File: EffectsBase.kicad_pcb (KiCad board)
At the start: 2 copper layers, 59 x 98 mm, 31 parts, among them J1 JACK CONNECTOR, J2 FOOTSWITCH, J3 PCIE_FX, Q1 SI2301BDS, SW1 SW_SPDT, SW2 SW_SPDT, SW3 MINI_SW, SW4 MINI_SW, U1 ICL7660S

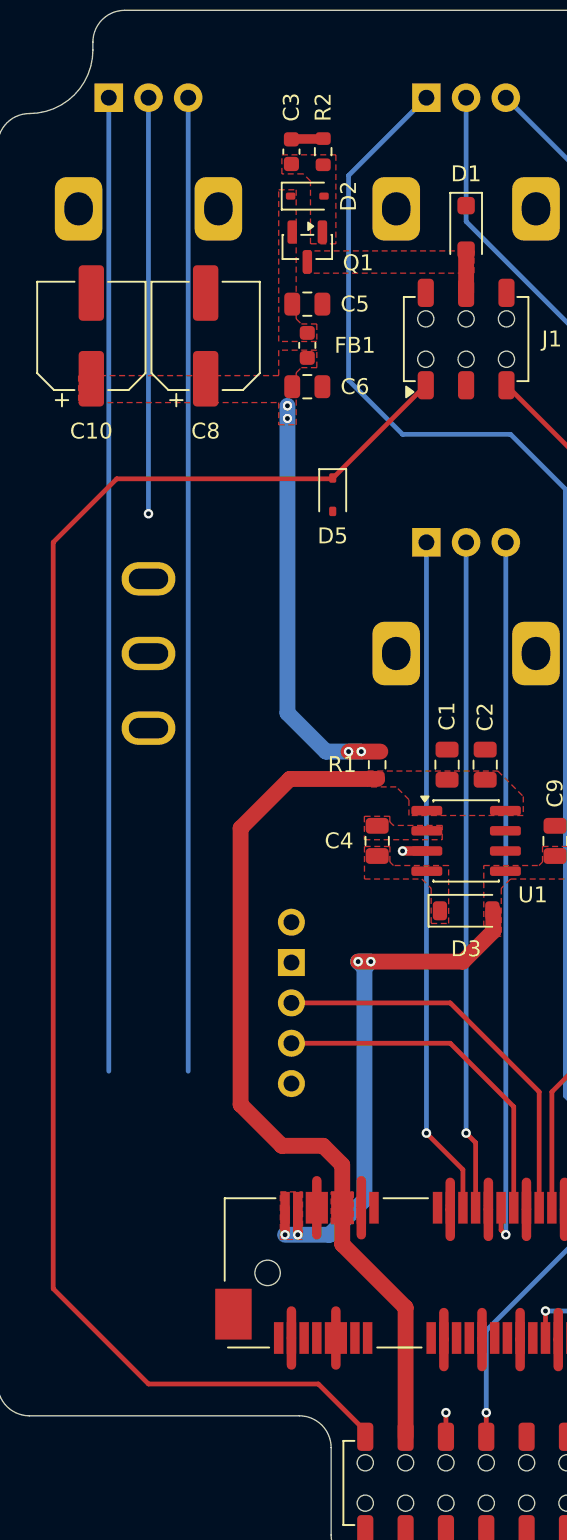
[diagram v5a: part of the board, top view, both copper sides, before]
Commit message: Board layout
Updated the layout of the power lines.
Updated the layout of the control signals.
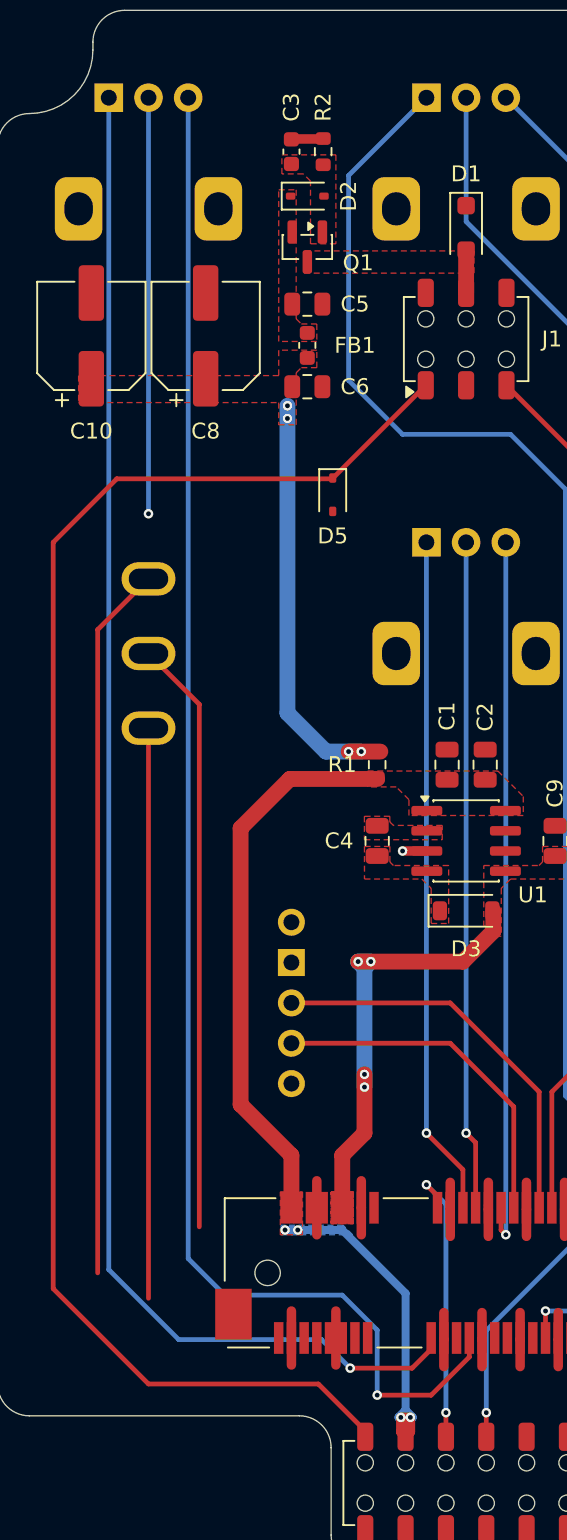
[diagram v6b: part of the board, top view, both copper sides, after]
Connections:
- J3 pad 10: +VCC_FILT -> -VSS
- J3 pad 12: +VCC_FILT -> -VSS
- J3 pad 2: -VSS -> +VCC_FILT
- J3 pad 29: /Controls/SW1_NC -> /Controls/SW1_NO
- J3 pad 33: /Controls/SW1_NO -> /Controls/SW1_NC
- J3 pad 4: -VSS -> +VCC_FILT
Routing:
- net /Controls/SW1_NC: track 0.00 -> 45.0 mm
- net /Controls/P1_L: track 61.3 -> 99.0 mm, vias 0 -> 1
- net /Controls/SW1_IN: track 0.00 -> 37.4 mm
- net /Controls/P1_H: track 61.3 -> 97.9 mm, vias 0 -> 1
- net /Controls/SW1_NO: track 0.00 -> 35.9 mm
- net /Controls/FX_IN: track 1.52 -> 18.1 mm, vias 1 -> 2
- net -VSS: track 36.4 -> 29.5 mm
- net +VCC_FILT: track 54.0 -> 57.5 mm, vias 0 -> 4
- added copper zone on B.Cu, net +VCC_FILT

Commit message: Layout and mounting
Connected all tracks in the layout.
Added a mounting standoff.
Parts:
- added H2: PCIE_MOUNT, Mounting_Wuerth:Mounting_Wuerth_WA-SMSI-M2_H1.5mm_9774015243, F.Cu at (150.0, 71.0)
- added REF**: Hammond_125B_1590N1_NOLID, Enclosures:Hammond_125B_1590N1_NOLID, B.Cu at (150.0, 100.0)
- J3: footprint Custom_Parts:Mini PCI_Express -> Custom_Parts:Mini PCI_Express_Pads
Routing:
- net /Controls/P1_W: track 26.2 -> 95.0 mm, vias 1 -> 3
- net /Controls/SW1_IN: track 37.4 -> 66.4 mm
- net /Controls/SW1_NO: track 35.9 -> 57.9 mm
- net /Controls/SW1_NC: track 45.0 -> 65.9 mm
- net /Controls/SW2_NO: track 46.6 -> 43.0 mm
- net /Controls/FX_IN: track 18.1 -> 15.2 mm
- net GND: track 58.4 -> 57.4 mm

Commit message: Finished layout
Initial PCB layout iteration.
Updated the readme file.
Added board images.
Added output files.
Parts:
- removed the J2 at (150.0, 135.2)
- added H2: TOOL, MountingHole:ToolingHole_1.152mm, F.Cu at (122.4, 51.0)
- added H3: TOOL, MountingHole:ToolingHole_1.152mm, F.Cu at (177.6, 51.0)
- added H4: TOOL, MountingHole:ToolingHole_1.152mm, F.Cu at (177.6, 129.0)
- added J1: FOOTSWITCH, Custom_Parts:HEADER_THROUGH_2x05_P2.54mm, F.Cu at (150.0, 135.3)
- renumbered H2 to H1, J1 to J2
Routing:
- net +VCC_FILT: track 57.5 -> 60.6 mm
- net -VSS: track 29.5 -> 26.4 mm, vias 4 -> 0
- net /Controls/AUDIO_IN: track 98.3 -> 99.6 mm
- net /Controls/AUDIO_OUT: track 98.3 -> 99.6 mm
- net /Controls/FX_IN: track 15.2 -> 14.4 mm
- net /Controls/SW3_NO: vias 0 -> 1
- net GND: vias 1 -> 204
- net /Controls/SW3_IN: vias 0 -> 1
- removed copper zone on B.Cu, net +VCC_FILT
